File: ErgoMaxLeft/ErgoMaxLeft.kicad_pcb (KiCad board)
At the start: 2 copper layers, 182.8 x 169.2 mm, 102 parts, among them J1 PJ-320A, K1 KEYSW, K10 KEYSW, K11 KEYSW, K12 KEYSW, K13 KEYSW, K14 KEYSW, K15 KEYSW, K16 KEYSW, K17 KEYSW, K18 KEYSW, K19 KEYSW, K2 KEYSW, K20 KEYSW, K21 KEYSW, K22 KEYSW, K23 KEYSW, K24 KEYSW, K25 KEYSW, K26 KEYSW, K27 KEYSW, K28 KEYSW, K29 KEYSW, K3 KEYSW, K30 KEYSW, K31 KEYSW, K32 KEYSW, K33 KEYSW, K34 KEYSW, K35 KEYSW, K36 KEYSW, K37 KEYSW, K38 KEYSW, K39 KEYSW, K4 KEYSW, K40 KEYSW, K41 KEYSW, K42 KEYSW, K43 KEYSW, K44 KEYSW, K5 KEYSW, K6 KEYSW, K7 KEYSW, K8 KEYSW, K9 KEYSW, U1 ProMicro

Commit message: cleanup diodes positions
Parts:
- moved D17 1.20 mm to (177.5, 101.4)
- moved D32 1.14 mm to (177.5, 139.5)
- moved D29 1.07 mm to (115.6, 144.3)
- moved D16 1.06 mm to (158.4, 103.0)
- moved D20 1.02 mm to (234.6, 109.0)
- moved D40 1.00 mm to (177.5, 158.5)
- moved D10 0.95 mm to (177.5, 82.3)
- moved D34 0.94 mm to (215.6, 142.4)
- moved D5 0.93 mm to (215.5, 66.2)
- moved D21 0.92 mm to (115.6, 125.2)
- moved D39 0.91 mm to (158.4, 160.1)
- moved D7 0.82 mm to (115.6, 87.1)
- moved D12 0.81 mm to (215.6, 85.2)
- moved D3 0.81 mm to (177.5, 63.3)
- moved D13 0.77 mm to (234.6, 85.2)
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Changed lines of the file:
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@@
   )
   (module Keebio-Parts:Diode_Long (layer B.Cu)
-    (at 196.80682 121.96572 270)
+    (at 196.523961 122.015005 270)
     (fp_text reference D25 (at 0 0 270) (layer B.SilkS)
       (effects (font (size 0.8 0.7) (thickness 0.15)) (justify mirror))
@@
   )
   (module Keebio-Parts:Diode_Long (layer B.Cu)
-    (at 216.25052 123.56338 270)
+    (at 215.573961 123.325845 270)
     (fp_text reference D26 (at 0 0 270) (layer B.SilkS)
       (effects (font (size 0.8 0.7) (thickness 0.15)) (justify mirror))
@@
   )
   (module Keebio-Parts:Diode_Long (layer B.Cu)
-    (at 114.57686 143.85544 270)
+    (at 115.563961 144.265005 270)
     (fp_text reference D29 (at 0 0 270) (layer B.SilkS)
       (effects (font (size 0.8 0.7) (thickness 0.15)) (justify mirror))
@@
   )
   (module Keebio-Parts:Diode_Long (layer B.Cu)
-    (at 139.38504 144.30248 270)
+    (at 139.373961 144.265005 270)
     (fp_text reference D30 (at 0 0 270) (layer B.SilkS)
       (effects (font (size 0.8 0.7) (thickness 0.15)) (justify mirror))
@@
   )
   (module Keebio-Parts:Diode_Long (layer B.Cu)
-    (at 158.74238 141.53642 270)
+    (at 158.423961 141.085005 270)
     (fp_text reference D31 (at 0 0 270) (layer B.SilkS)
       (effects (font (size 0.8 0.7) (thickness 0.15)) (justify mirror))
@@
   )
   (module Keebio-Parts:Diode_Long (layer B.Cu)
-    (at 178.33594 140.22832 270)
+    (at 177.473961 139.475005 270)
     (fp_text reference D32 (at 0 0 270) (layer B.SilkS)
       (effects (font (size 0.8 0.7) (thickness 0.15)) (justify mirror))
@@
   )
   (module Keebio-Parts:Diode_Long (layer B.Cu)
-    (at 196.94652 141.28496 270)
+    (at 196.523961 141.055005 270)
     (fp_text reference D33 (at 0 0 270) (layer B.SilkS)
       (effects (font (size 0.8 0.7) (thickness 0.15)) (justify mirror))
@@
   )
   (module Keebio-Parts:Diode_Long (layer B.Cu)
-    (at 216.3826 142.83182 270)
+    (at 215.573961 142.355005 270)
     (fp_text reference D34 (at 0 0 270) (layer B.SilkS)
       (effects (font (size 0.8 0.7) (thickness 0.15)) (justify mirror))
@@
   )
   (module Keebio-Parts:Diode_Long (layer B.Cu)
-    (at 216.25052 85.68182 270)
+    (at 215.573961 85.228525 270)
     (fp_text reference D12 (at 0 0 270) (layer B.SilkS)
       (effects (font (size 0.8 0.7) (thickness 0.15)) (justify mirror))
@@
   )
   (module Keebio-Parts:Diode_Long (layer B.Cu)
-    (at 158.94304 160.86074 270)
+    (at 158.423961 160.115005 270)
     (fp_text reference D39 (at 0 0 270) (layer B.SilkS)
       (effects (font (size 0.8 0.7) (thickness 0.15)) (justify mirror))
@@
   )
   (module Keebio-Parts:Diode_Long (layer B.Cu)
-    (at 178.13782 159.26054 270)
+    (at 177.473961 158.515005 270)
     (fp_text reference D40 (at 0 0 270) (layer B.SilkS)
       (effects (font (size 0.8 0.7) (thickness 0.15)) (justify mirror))
@@
   )
   (module Keebio-Parts:Diode_Long (layer B.Cu)
-    (at 196.94652 160.46196 270)
+    (at 196.523961 160.095005 270)
     (fp_text reference D41 (at 0 0 270) (layer B.SilkS)
       (effects (font (size 0.8 0.7) (thickness 0.15)) (justify mirror))
@@
   )
   (module Keebio-Parts:Diode_Long (layer B.Cu)
-    (at 222.24746 166.40556 65)
+    (at 222.80626 166.78656 65)
     (fp_text reference D42 (at 0 0 65) (layer B.SilkS)
       (effects (font (size 0.8 0.7) (thickness 0.15)) (justify mirror))
@@
   )
   (module Keebio-Parts:Diode_Long (layer B.Cu)
-    (at 139.46124 125.37694 270)
+    (at 139.365561 125.227045 270)
     (fp_text reference D22 (at 0 0 270) (layer B.SilkS)
       (effects (font (size 0.8 0.7) (thickness 0.15)) (justify mirror))
@@
   )
   (module Keebio-Parts:Diode_Long (layer B.Cu)
-    (at 158.60776 65.51168 270)
+    (at 158.413961 64.892045 270)
     (fp_text reference D2 (at 0 0 270) (layer B.SilkS)
       (effects (font (size 0.8 0.7) (thickness 0.15)) (justify mirror))
@@
   )
   (module Keebio-Parts:Diode_Long (layer B.Cu)
-    (at 178.00574 63.89116 270)
+    (at 177.453961 63.294645 270)
     (fp_text reference D3 (at 0 0 270) (layer B.SilkS)
       (effects (font (size 0.8 0.7) (thickness 0.15)) (justify mirror))
@@
   )
   (module Keebio-Parts:Diode_Long (layer B.Cu)
-    (at 196.94652 65.2653 270)
+    (at 196.493961 64.878645 270)
     (fp_text reference D4 (at 0 0 270) (layer B.SilkS)
       (effects (font (size 0.8 0.7) (thickness 0.15)) (justify mirror))
@@
   )
   (module Keebio-Parts:Diode_Long (layer B.Cu)
-    (at 216.3826 66.54546 270)
+    (at 215.531712 66.178645 270)
     (fp_text reference D5 (at 0 0 270) (layer B.SilkS)
       (effects (font (size 0.8 0.7) (thickness 0.15)) (justify mirror))
@@
   )
   (module Keebio-Parts:Diode_Long (layer B.Cu)
-    (at 234.99572 66.41338 270)
+    (at 234.623961 66.180645 270)
     (fp_text reference D6 (at 0 0 270) (layer B.SilkS)
       (effects (font (size 0.8 0.7) (thickness 0.15)) (justify mirror))
@@
   )
   (module Keebio-Parts:Diode_Long (layer B.Cu)
-    (at 114.80292 86.80704 270)
+    (at 115.555641 87.135645 270)
     (fp_text reference D7 (at 0 0 270) (layer B.SilkS)
       (effects (font (size 0.8 0.7) (thickness 0.15)) (justify mirror))
@@
   )
   (module Keebio-Parts:Diode_Long (layer B.Cu)
-    (at 139.0904 87.49538 270)
+    (at 139.361061 87.135645 270)
     (fp_text reference D8 (at 0 0 270) (layer B.SilkS)
       (effects (font (size 0.8 0.7) (thickness 0.15)) (justify mirror))
@@
   )
   (module Keebio-Parts:Diode_Long (layer B.Cu)
-    (at 158.60776 84.0994 270)
+    (at 158.411061 83.945645 270)
     (fp_text reference D9 (at 0 0 270) (layer B.SilkS)
       (effects (font (size 0.8 0.7) (thickness 0.15)) (justify mirror))
@@
   )
   (module Keebio-Parts:Diode_Long (layer B.Cu)
-    (at 178.07178 83.058 270)
+    (at 177.456661 82.340085 270)
     (fp_text reference D10 (at 0 0 270) (layer B.SilkS)
       (effects (font (size 0.8 0.7) (thickness 0.15)) (justify mirror))
@@
   )
   (module Keebio-Parts:Diode_Long (layer B.Cu)
-    (at 158.74238 122.27814 270)
+    (at 158.423961 122.035245 270)
     (fp_text reference D23 (at 0 0 270) (layer B.SilkS)
       (effects (font (size 0.8 0.7) (thickness 0.15)) (justify mirror))
@@
   )
   (module Keebio-Parts:Diode_Long (layer B.Cu)
-    (at 178.20386 120.53316 270)
+    (at 177.473961 120.432245 270)
     (fp_text reference D24 (at 0 0 270) (layer B.SilkS)
       (effects (font (size 0.8 0.7) (thickness 0.15)) (justify mirror))
@@
   )
   (module Keebio-Parts:Diode_Long (layer B.Cu)
-    (at 235.32338 85.54974 270)
+    (at 234.623961 85.220945 270)
     (fp_text reference D13 (at 0 0 270) (layer B.SilkS)
       (effects (font (size 0.8 0.7) (thickness 0.15)) (justify mirror))
@@
   )
   (module Keebio-Parts:Diode_Long (layer B.Cu)
-    (at 114.8969 105.8291 270)
+    (at 115.559041 106.178745 270)
     (fp_text reference D14 (at 0 0 270) (layer B.SilkS)
       (effects (font (size 0.8 0.7) (thickness 0.15)) (justify mirror))
@@
   )
   (module Keebio-Parts:Diode_Long (layer B.Cu)
-    (at 139.51458 106.71302 270)
+    (at 139.359821 106.188345 270)
     (fp_text reference D15 (at 0 0 270) (layer B.SilkS)
       (effects (font (size 0.8 0.7) (thickness 0.15)) (justify mirror))
@@
   )
   (module Keebio-Parts:Diode_Long (layer B.Cu)
-    (at 159.34436 103.48976 270)
+    (at 158.408561 102.987625 270)
     (fp_text reference D16 (at 0 0 270) (layer B.SilkS)
       (effects (font (size 0.8 0.7) (thickness 0.15)) (justify mirror))
@@
   )
   (module Keebio-Parts:Diode_Long (layer B.Cu)
-    (at 178.46802 102.02672 270)
+    (at 177.453001 101.384545 270)
     (fp_text reference D17 (at 0 0 270) (layer B.SilkS)
       (effects (font (size 0.8 0.7) (thickness 0.15)) (justify mirror))
@@
   )
   (module Keebio-Parts:Diode_Long (layer B.Cu)
-    (at 197.0151 103.34498 270)
+    (at 196.498401 102.970265 270)
     (fp_text reference D18 (at 0 0 270) (layer B.SilkS)
       (effects (font (size 0.8 0.7) (thickness 0.15)) (justify mirror))
@@
   )
   (module Keebio-Parts:Diode_Long (layer B.Cu)
-    (at 216.12098 104.75468 270)
+    (at 215.531561 104.281045 270)
     (fp_text reference D19 (at 0 0 270) (layer B.SilkS)
       (effects (font (size 0.8 0.7) (thickness 0.15)) (justify mirror))
@@
   )
   (module Keebio-Parts:Diode_Long (layer B.Cu)
-    (at 235.32338 109.78388 270)
+    (at 234.623961 109.040645 270)
     (fp_text reference D20 (at 0 0 270) (layer B.SilkS)
       (effects (font (size 0.8 0.7) (thickness 0.15)) (justify mirror))
@@
   )
   (module Keebio-Parts:Diode_Long (layer B.Cu)
-    (at 114.681 124.97054 270)
+    (at 115.569361 125.218845 270)
     (fp_text reference D21 (at 0 0 270) (layer B.SilkS)
       (effects (font (size 0.8 0.7) (thickness 0.15)) (justify mirror))
@@
   )
   (module Keebio-Parts:Diode_Long (layer B.Cu)
-    (at 196.59854 84.16544 270)
+    (at 196.498561 83.932425 270)
     (fp_text reference D11 (at 0 0 270) (layer B.SilkS)
       (effects (font (size 0.8 0.7) (thickness 0.15)) (justify mirror))

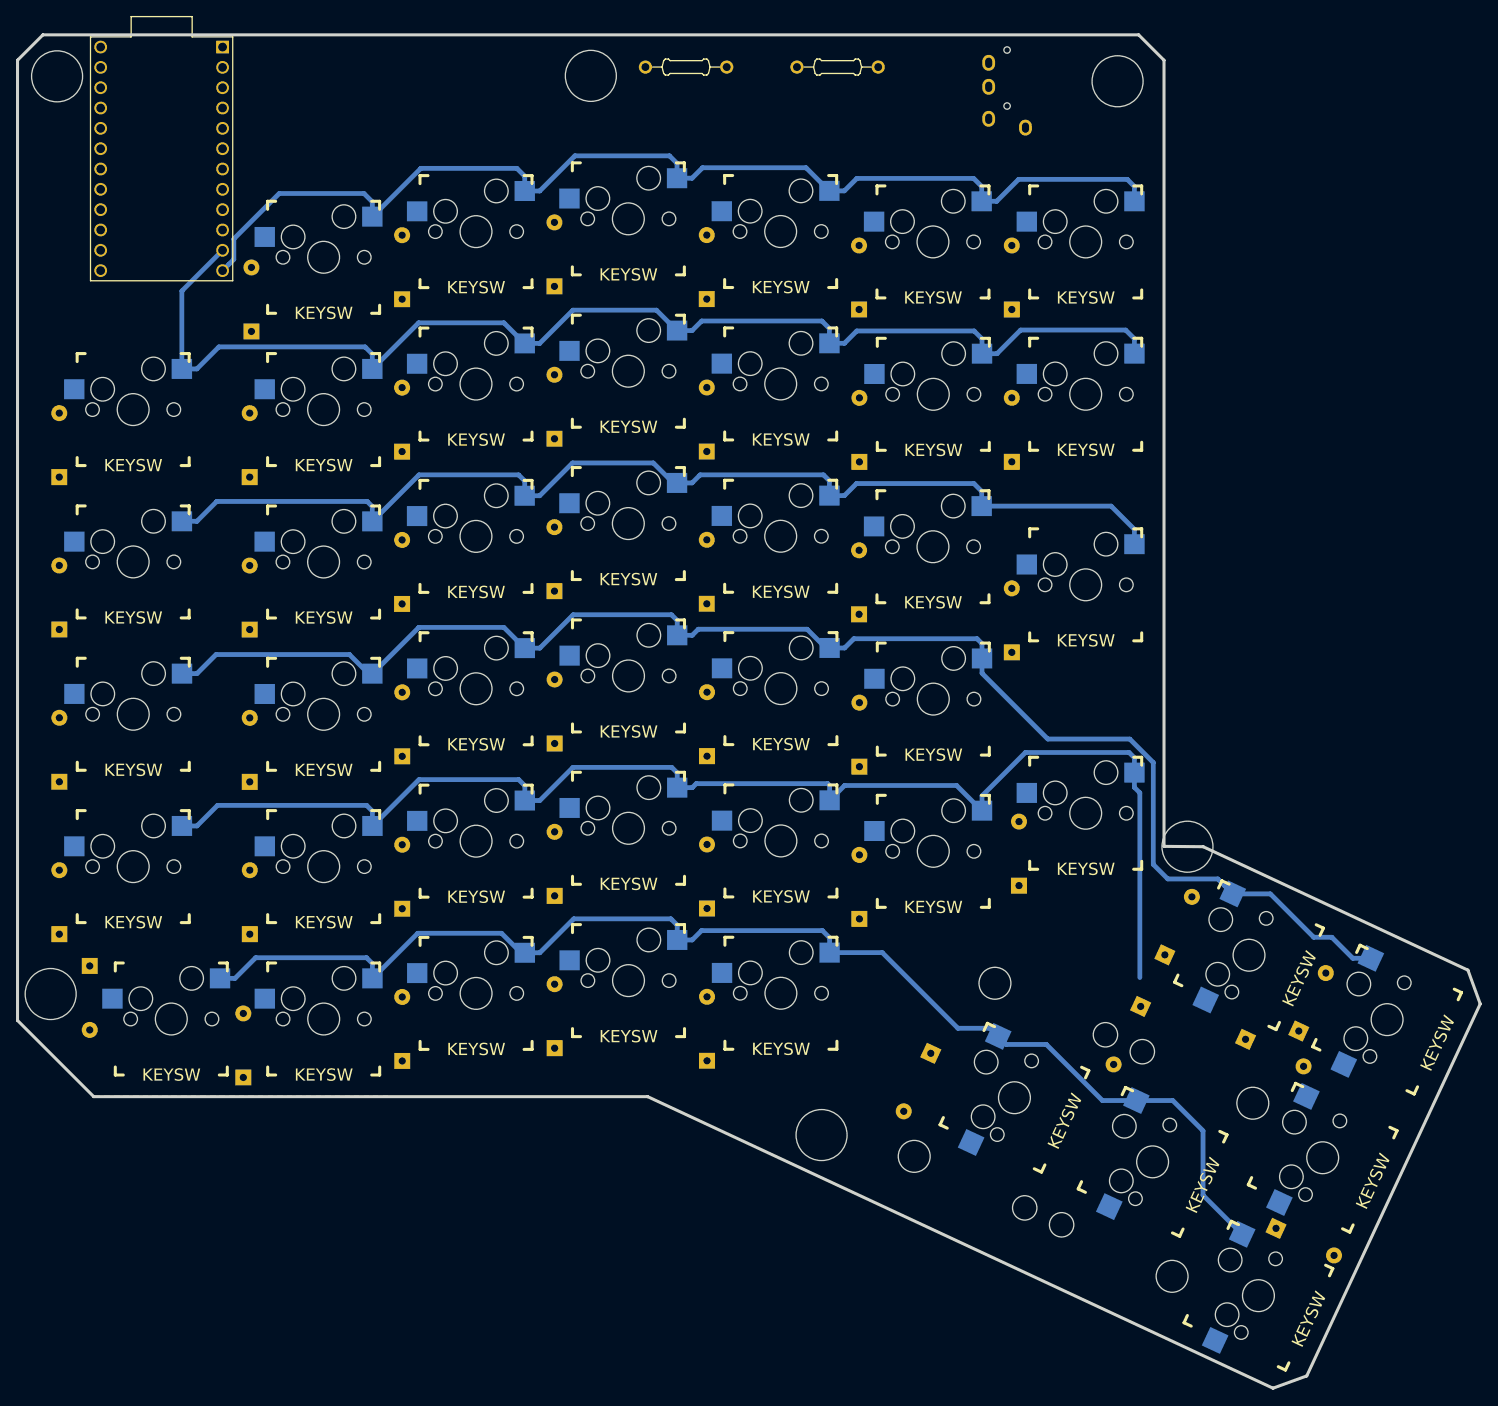
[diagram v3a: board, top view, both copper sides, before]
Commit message: add more wiring - wiring columns is going to cause some problems
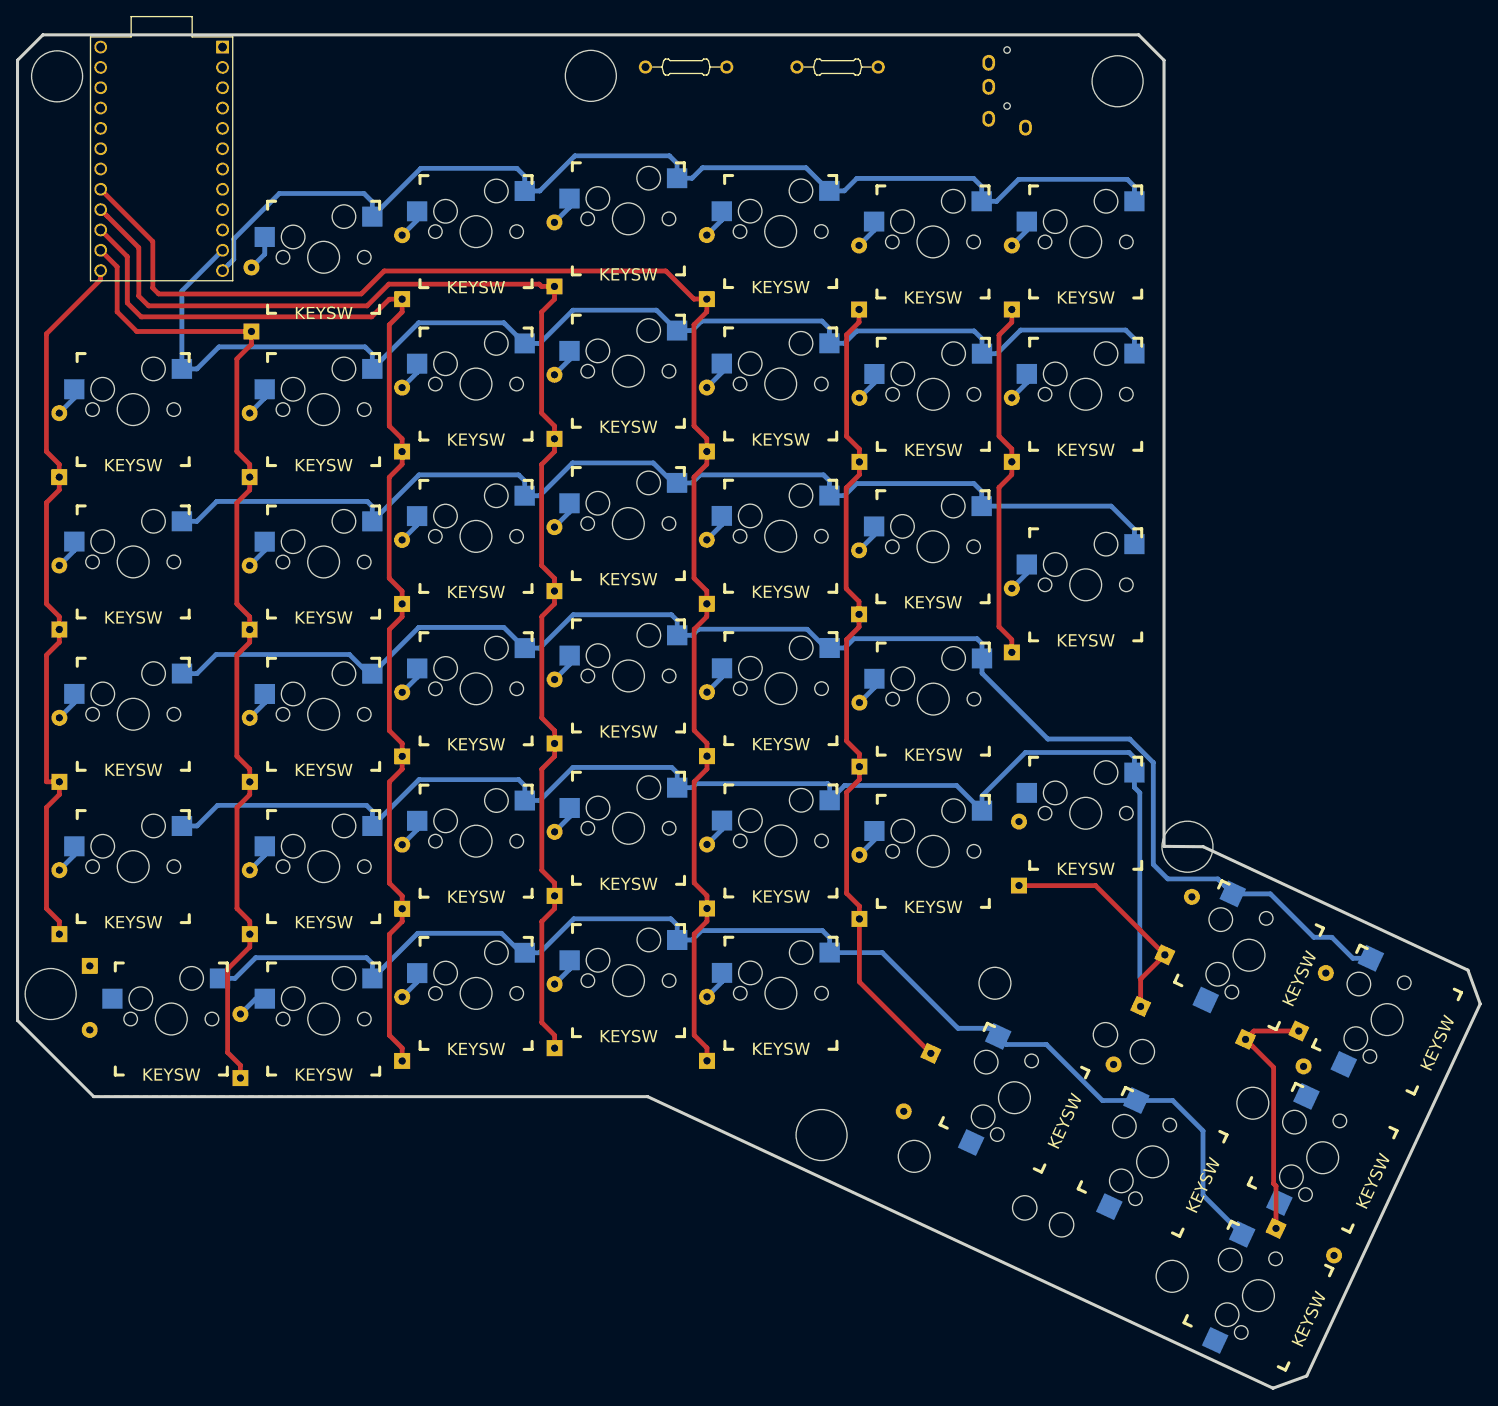
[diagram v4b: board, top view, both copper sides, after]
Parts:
- moved D38 0.37 mm to (138.2, 162.3)
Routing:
- net /Col4: track 0.00 -> 189.1 mm
- net /Col3: track 0.00 -> 168.4 mm
- net /Col2: track 0.00 -> 148.4 mm
- net /Col1: track 0.00 -> 126.9 mm
- net /Col5: track 0.00 -> 102.0 mm
- net /Col0: track 0.00 -> 91.3 mm
- net /Col6: track 0.00 -> 75.0 mm
- net /Col7: track 0.00 -> 32.3 mm
- net Net-(D1-Pad2): track 0.00 -> 4.50 mm
- net Net-(D38-Pad2): track 0.00 -> 3.85 mm
- net Net-(D39-Pad2): track 0.00 -> 3.76 mm
- net Net-(D31-Pad2): track 0.00 -> 3.76 mm
- net Net-(D16-Pad2): track 0.00 -> 3.76 mm
- net Net-(D9-Pad2): track 0.00 -> 3.76 mm
- net Net-(D3-Pad2): track 0.00 -> 3.76 mm
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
